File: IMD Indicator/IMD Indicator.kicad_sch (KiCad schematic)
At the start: 15 parts, among them J1 172448-0004, J2 172448-0004, J3 172448-0004, Q1 2N7002,215, Q2 2N7002,215

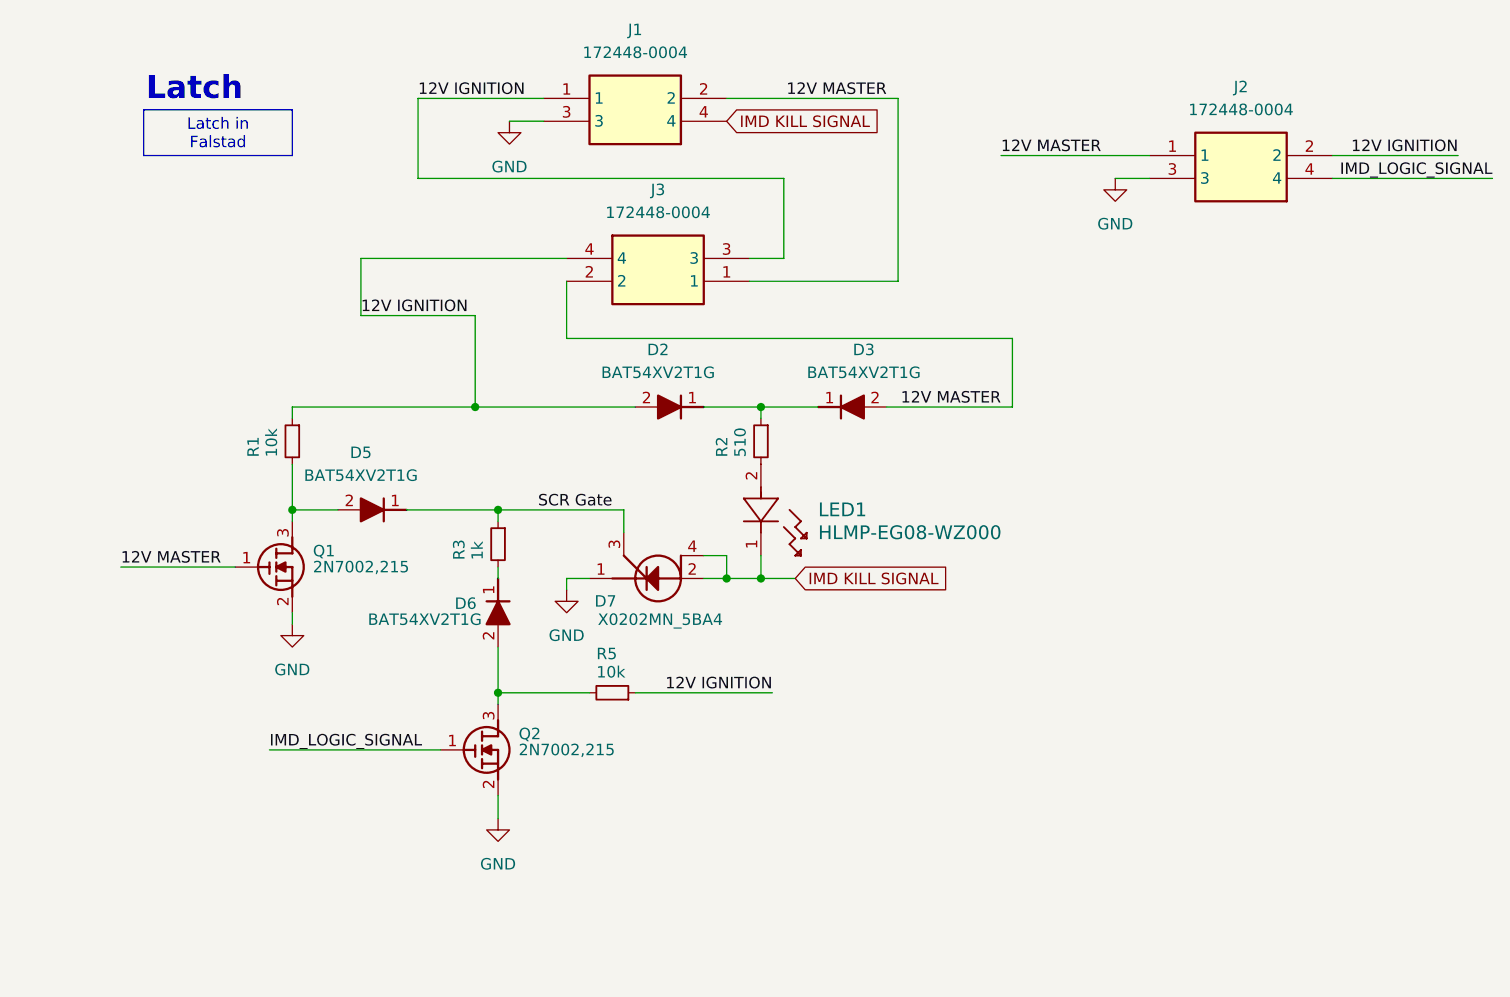
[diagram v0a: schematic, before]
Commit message: updated datasheets, part numbers, and price/stock
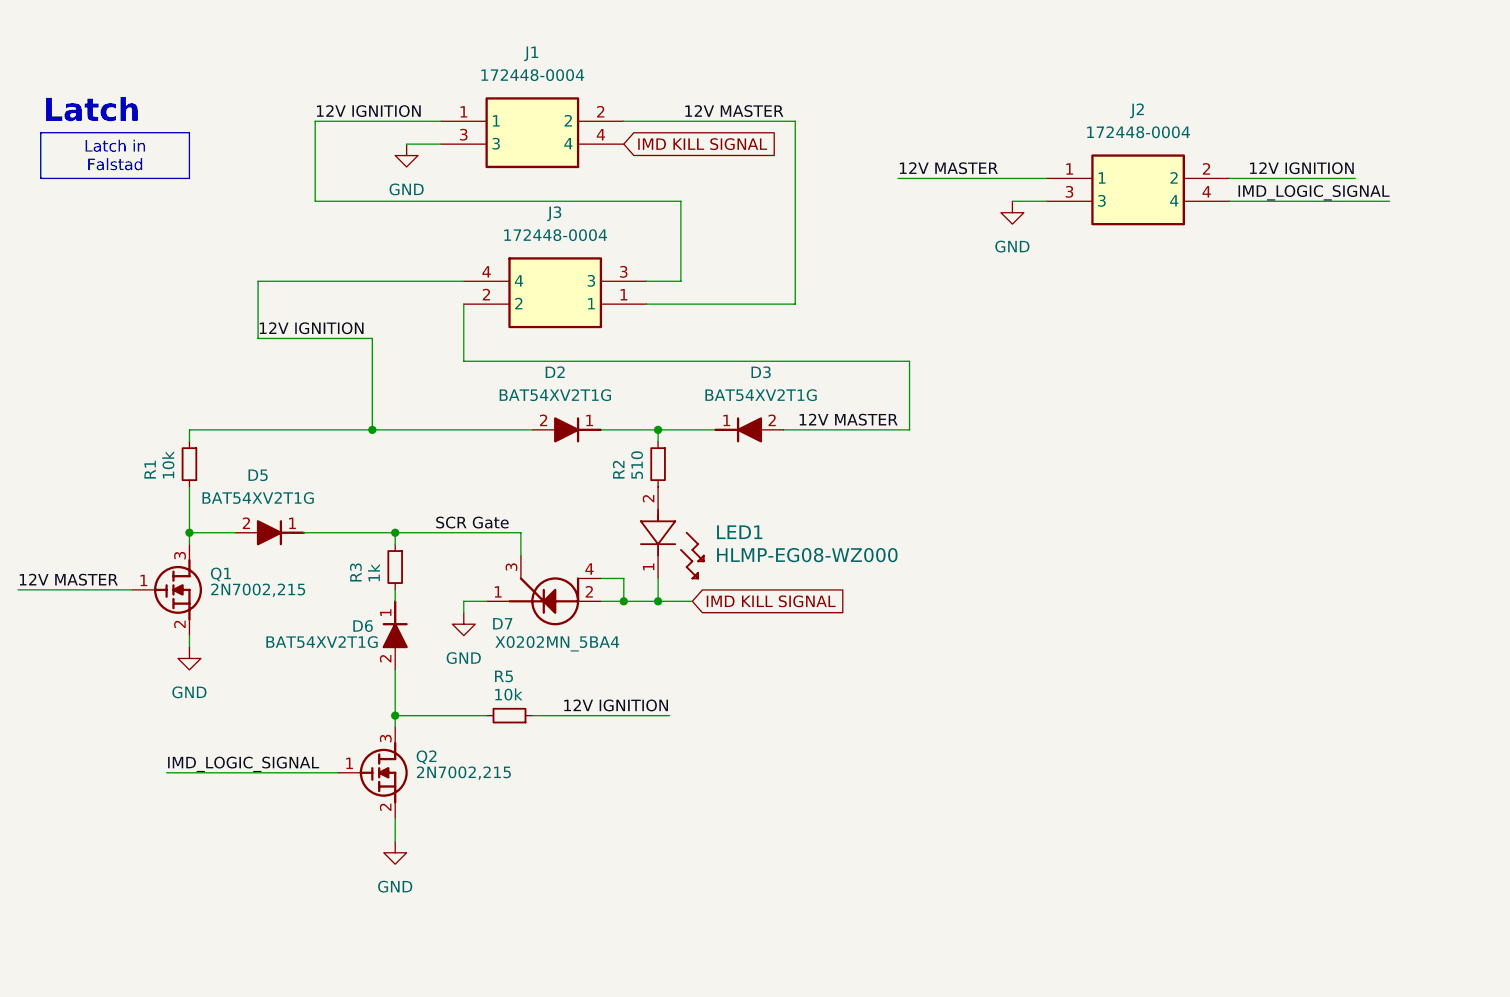
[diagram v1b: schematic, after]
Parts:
- LED1: Mouser Part Number (none) -> 630-HLMP-EG08-WZ000; Mouser Price/Stock (none) -> https://www.mouser.com/ProductDetail/Broadcom-Avago/HLMP-EG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
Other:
- moved on the sheet: D2, D3, D5, D6, D7, J1, J2, J3, LED1, Q1, Q2, R1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

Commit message: changed LED (symbol, footprint)
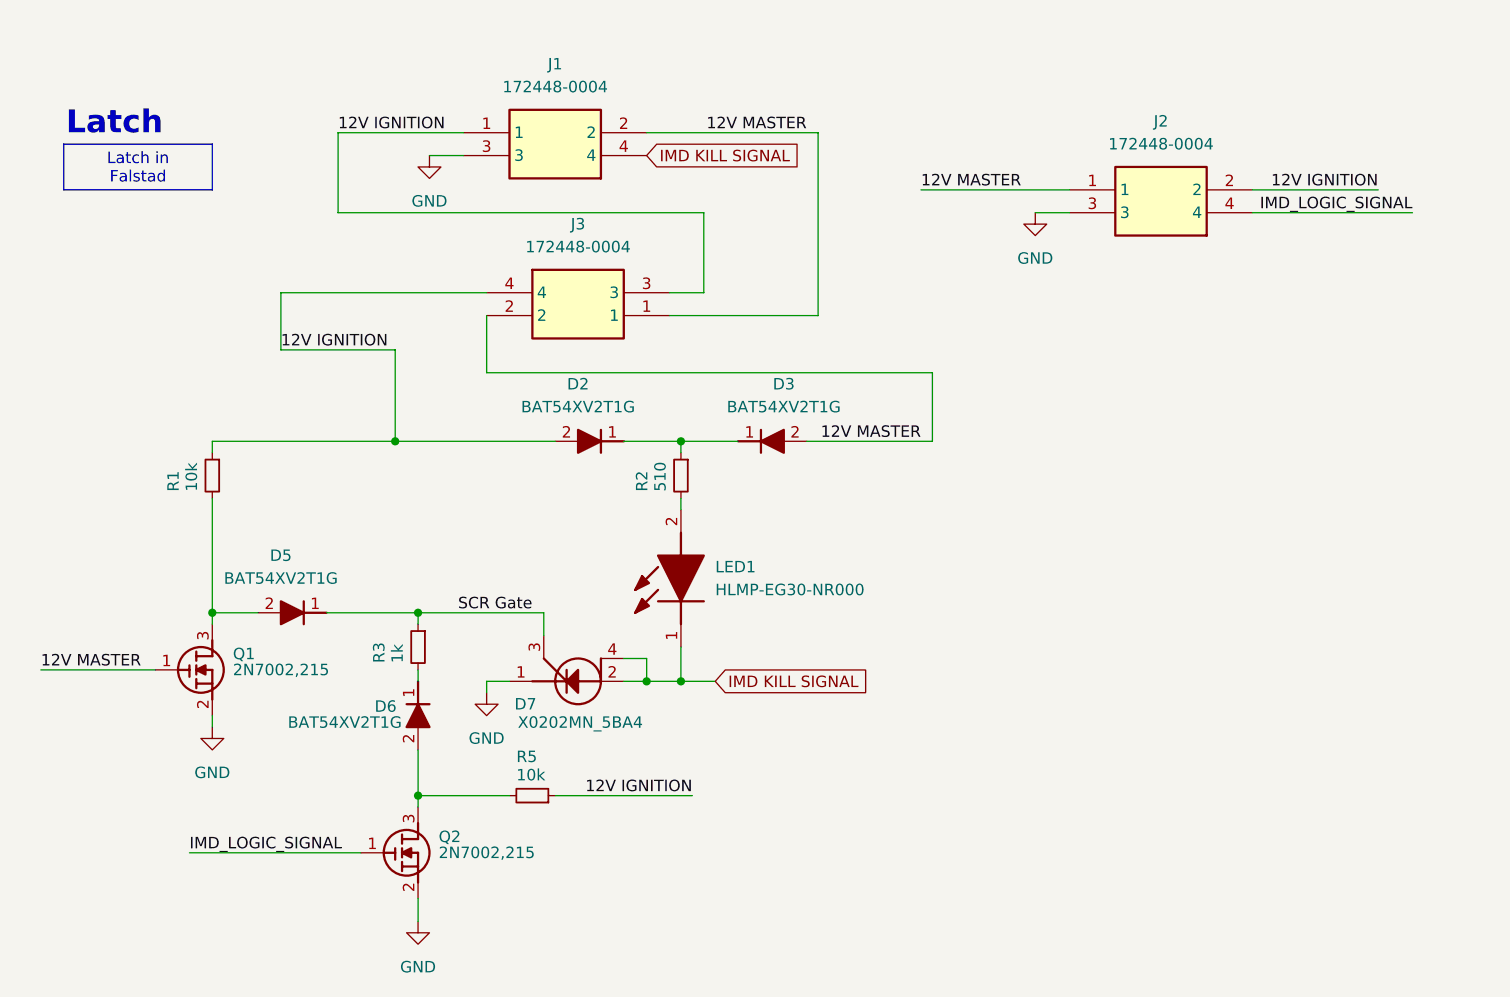
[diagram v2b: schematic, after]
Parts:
- removed LED1: HLMP-EG08-WZ000, IMDFootprintLibrary:LED_-WZ000, symbol IMDSymbolLibrary:HLMP-EG08-WZ000
- added LED1: HLMP-EG30-NR000, IMDFootprintLibrary:LED_5MM, symbol IMDSymbolLibrary:HLMP-EG30-NR000
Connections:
- net IMD KILL SIGNAL: now also LED1.1 (K)
- net at R2.2: now also LED1.2 (A)
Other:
- moved on the sheet: D2, D3, D5, D6, D7, J1, J2, J3, Q1, Q2, R1, R2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

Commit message: removed unnecessary connectors from sch & layout, added pulldown resistor
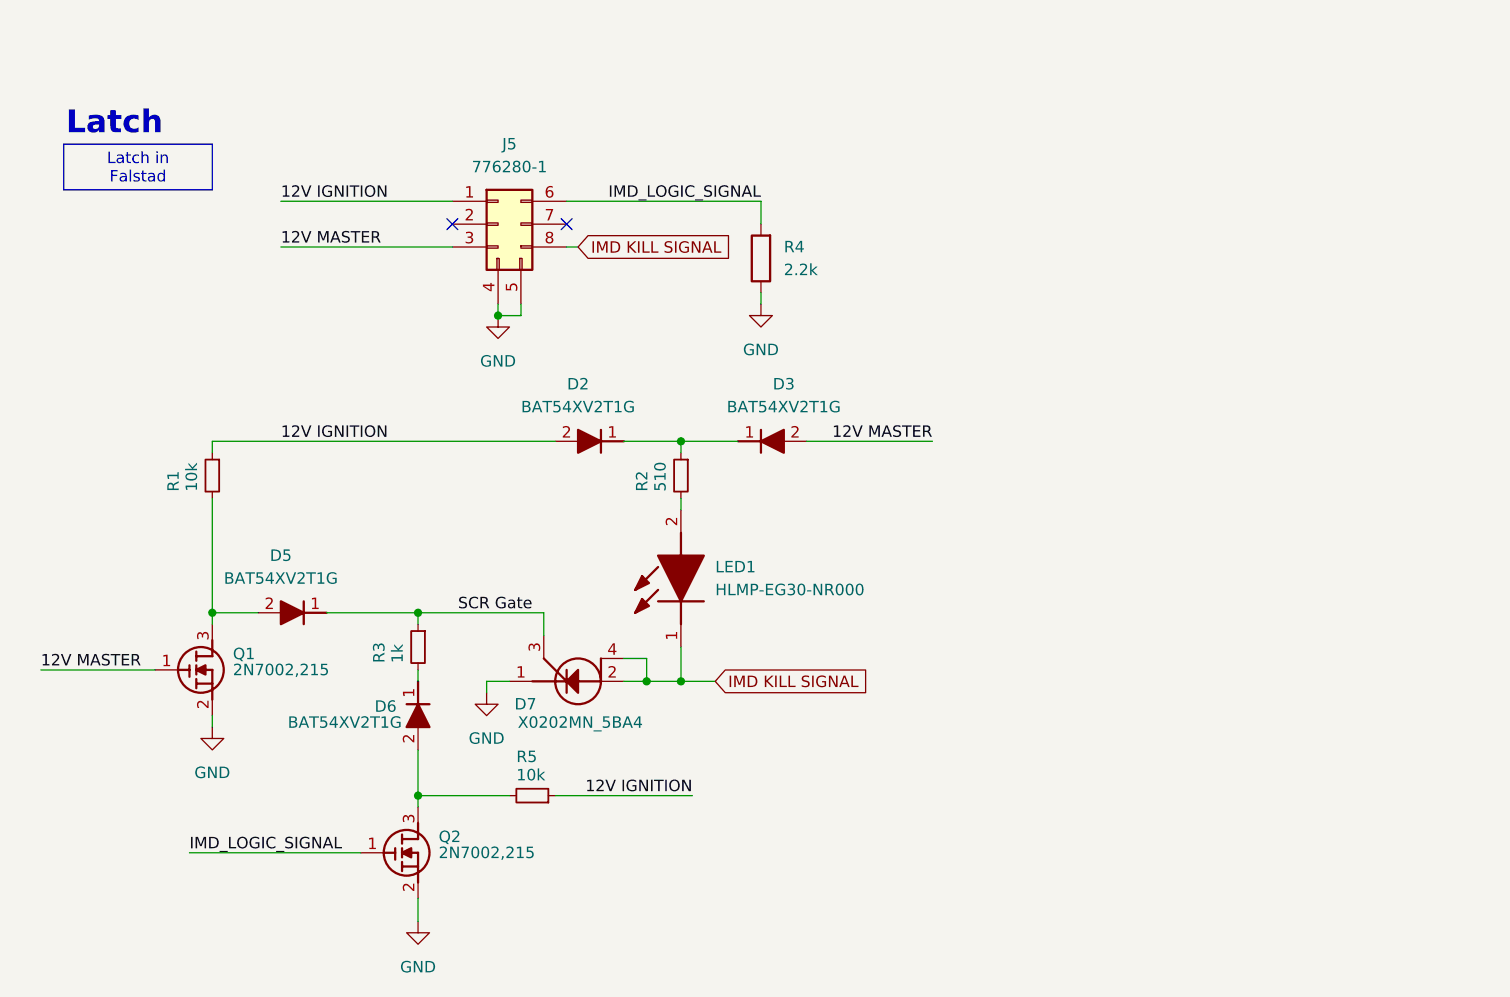
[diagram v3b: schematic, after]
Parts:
- removed J1, J2, J3: 172448-0004, IMDFootprintLibrary:172448-YY04, symbol IMDSymbolLibrary:172448-0004
- added J5: 776280-1, SDM_MiscFootprint:776280-1, symbol IMDSymbolLibrary:776280-1
- added R4: 2.2k, Resistor_SMD:R_0603_1608Metric, symbol Device:R
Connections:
- net 12V IGNITION: now also J5.1 (Pin_1)
- net 12V MASTER: now also J5.3 (Pin_3)
- net GND: now also J5.4 (Pin_4), J5.5 (Pin_5), R4.1
- net IMD KILL SIGNAL: now also J5.8 (Pin_8)
- net IMD_LOGIC_SIGNAL: now also J5.6 (Pin_6), R4.2
- no-connect marks 0 -> 2
